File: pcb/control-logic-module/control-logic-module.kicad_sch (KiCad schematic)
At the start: 47 parts, among them U1 74HC04, U2 74AHC1G00, U3 74AHC1G00, U4 TLC556, U5 74LS145, Y1 8MHz

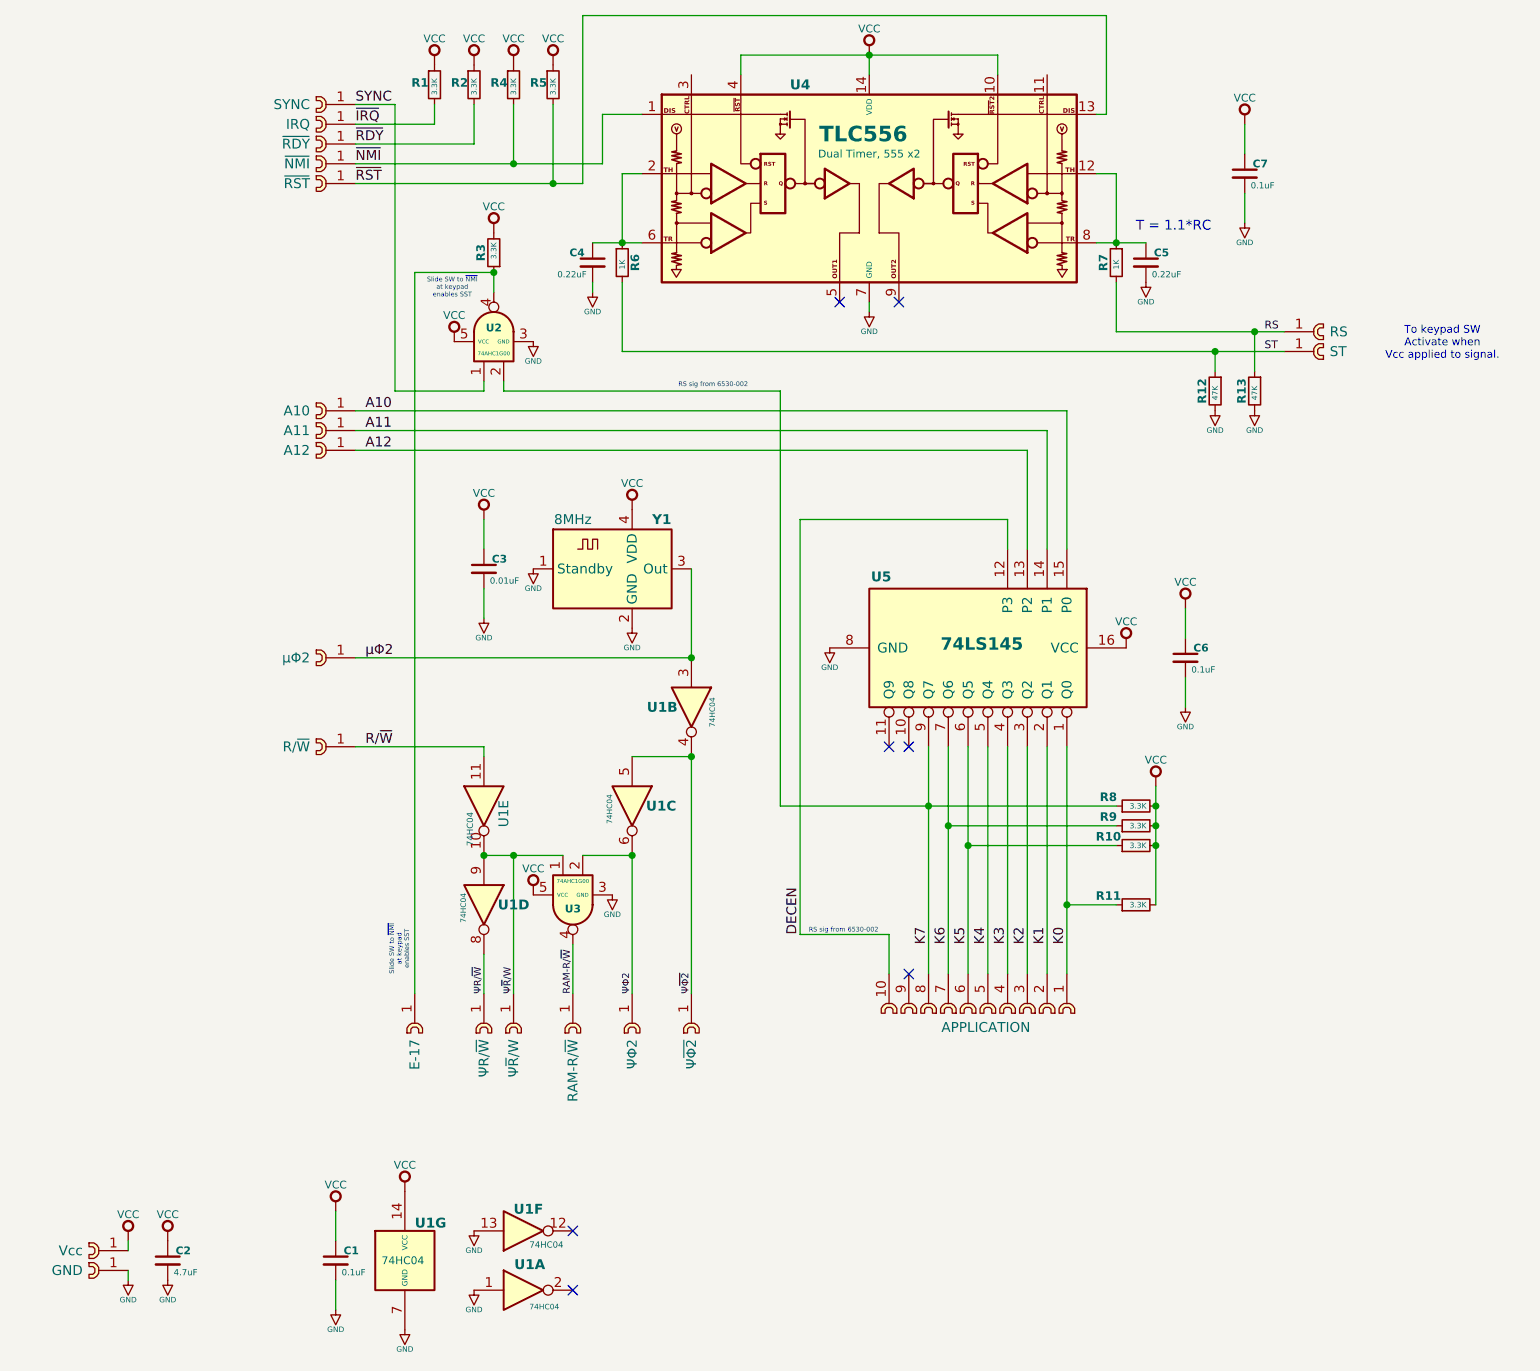
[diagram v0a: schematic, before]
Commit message: Fix ERC Errors
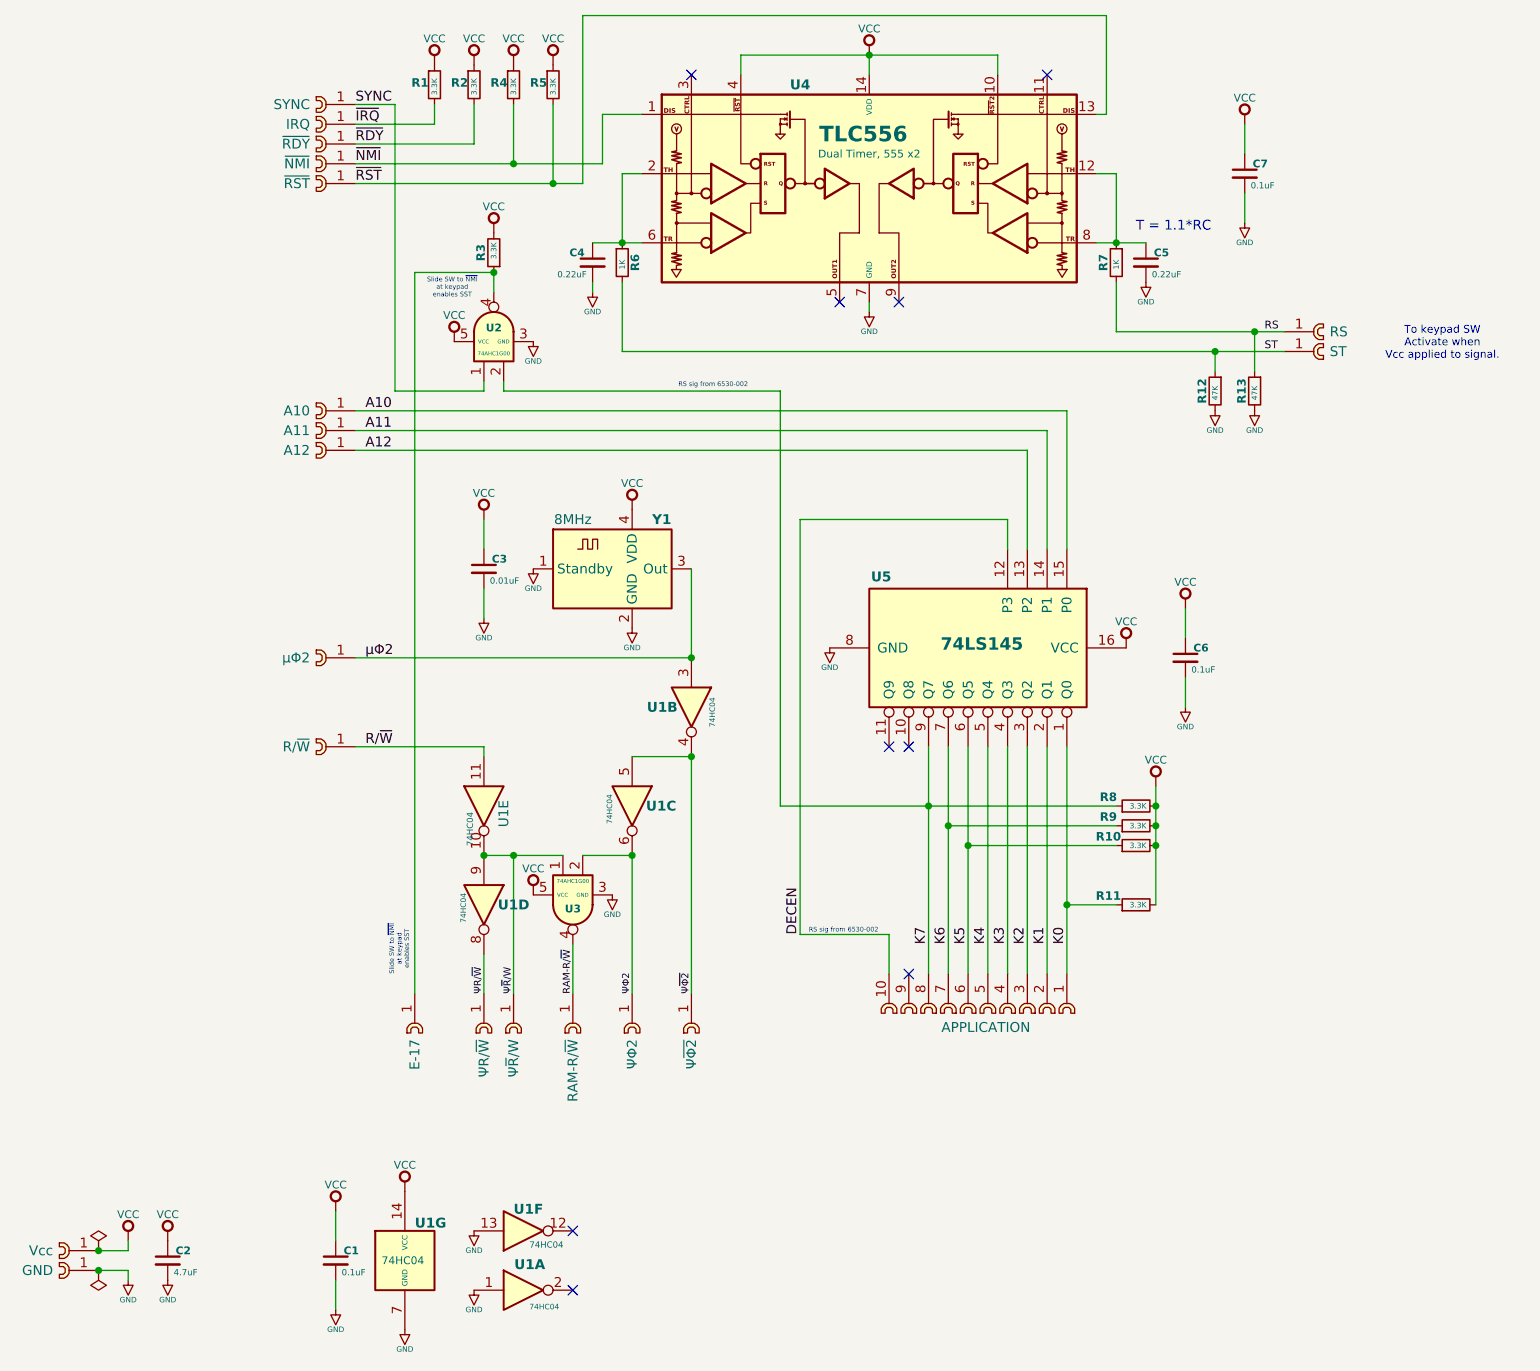
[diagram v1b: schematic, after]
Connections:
- no-connect marks 7 -> 9
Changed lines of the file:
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@@
 	)
 	(junction
+		(at 63.5 182.88)
+		(diameter 0)
+		(color 0 0 0 0)
+	)
+	(junction
 		(at 175.26 128.27)
 		(diameter 0)
@@
 	)
 	(junction
+		(at 63.5 180.34)
+		(diameter 0)
+		(color 0 0 0 0)
+	)
+	(junction
 		(at 113.03 129.54)
 		(diameter 0)
@@
 	)
 	(no_connect
+		(at 139.7 29.21)
+	)
+	(no_connect
 		(at 165.1 115.57)
 	)
@@
 	)
 	(no_connect
+		(at 185.42 29.21)
+	)
+	(no_connect
 		(at 124.46 177.8)
 	)
@@
 	(wire
 		(pts
-			(xy 67.31 184.15) (xy 67.31 182.88)
+			(xy 93.98 184.15) (xy 93.98 187.96)
 		)
 		(stroke
@@
 	(wire
 		(pts
-			(xy 93.98 184.15) (xy 93.98 187.96)
+			(xy 130.81 64.77) (xy 207.01 64.77)
 		)
 		(stroke
@@
 	(wire
 		(pts
-			(xy 130.81 64.77) (xy 207.01 64.77)
+			(xy 67.31 180.34) (xy 67.31 179.07)
 		)
 		(stroke
@@
 	(wire
 		(pts
+			(xy 67.31 182.88) (xy 67.31 184.15)
+		)
+		(stroke
+			(width 0)
+			(type default)
+		)
+	)
+	(wire
+		(pts
 			(xy 128.27 34.29) (xy 128.27 40.64)
 		)
@@
 	(wire
 		(pts
+			(xy 63.5 182.88) (xy 67.31 182.88)
+		)
+		(stroke
+			(width 0)
+			(type default)
+		)
+	)
+	(wire
+		(pts
 			(xy 182.88 77.47) (xy 182.88 90.17)
 		)
@@
 	(wire
 		(pts
+			(xy 63.5 180.34) (xy 67.31 180.34)
+		)
+		(stroke
+			(width 0)
+			(type default)
+		)
+	)
+	(wire
+		(pts
 			(xy 180.34 90.17) (xy 180.34 86.36)
 		)
@@
 	(wire
 		(pts
-			(xy 67.31 179.07) (xy 67.31 180.34)
-		)
-		(stroke
-			(width 0)
-			(type default)
-		)
-	)
-	(wire
-		(pts
 			(xy 106.68 33.02) (xy 106.68 35.56)
 		)
@@
 	)
 	(symbol
+		(lib_id "power:PWR_FLAG")
+		(at 63.5 180.34 0)
+		(unit 1)
+		(exclude_from_sim no)
+		(in_bom yes)
+		(on_board yes)
+		(dnp no)
+		(fields_autoplaced yes)
+		(property "Reference" "#FLG01"
+			(at 63.5 178.435 0)
+			(effects
+				(font
+					(size 1.27 1.27)
+				)
+				(hide yes)
+			)
+		)
+		(property "Value" "PWR_FLAG"
+			(at 63.5 175.26 0)
+			(effects
+				(font
+					(size 1.27 1.27)
+				)
+				(hide yes)
+			)
+		)
+		(property "Footprint" ""
+			(at 63.5 180.34 0)
+			(effects
+				(font
+					(size 1.27 1.27)
+				)
+				(hide yes)
+			)
+		)
+		(property "Datasheet" "~"
+			(at 63.5 180.34 0)
+			(effects
+				(font
+					(size 1.27 1.27)
+				)
+				(hide yes)
+			)
+		)
+		(property "Description" "Special symbol for telling ERC where power comes from"
+			(at 63.5 180.34 0)
+			(effects
+				(font
+					(size 1.27 1.27)
+				)
+				(hide yes)
+			)
+		)
+		(pin "1"
+		)
+		(instances
+			(project ""
+				(path "/4ebd6183-7c5f-46b0-b04d-0ff005f0292d"
+					(reference "#FLG01")
+					(unit 1)
+				)
+			)
+		)
+	)
+	(symbol
 		(lib_id "CM_power:VCC")
 		(at 114.3 49.53 0)
@@
 	(symbol
 		(lib_id "CM_Connector_Generic:cast-01")
-		(at 64.77 180.34 0)
+		(at 60.96 180.34 0)
 		(unit 1)
 		(exclude_from_sim no)
@@
 		(dnp no)
 		(property "Reference" "CST1"
-			(at 59.69 180.34 0)
+			(at 55.88 180.34 0)
 			(do_not_autoplace yes)
 			(effects
@@
 		)
 		(property "Value" "Vcc"
-			(at 61.468 180.34 0)
+			(at 57.658 180.34 0)
 			(effects
 				(font
@@
 		)
 		(property "Footprint" "CM_Connector_Castelated:cast-2.0-01P"
-			(at 57.15 180.34 0)
+			(at 53.34 180.34 0)
 			(do_not_autoplace yes)
 			(effects
@@
 		)
 		(property "Datasheet" ""
-			(at 64.77 180.34 0)
+			(at 60.96 180.34 0)
 			(effects
 				(font
@@
 		)
 		(property "Description" "Castelated PCB Edge - 2.0mm - 1P"
-			(at 57.15 179.07 0)
+			(at 53.34 179.07 0)
 			(do_not_autoplace yes)
 			(effects
@@
 	(symbol
 		(lib_id "CM_Connector_Generic:cast-01")
-		(at 64.77 182.88 0)
+		(at 60.96 182.88 0)
 		(unit 1)
 		(exclude_from_sim no)
@@
 		(dnp no)
 		(property "Reference" "CST2"
-			(at 59.69 182.88 0)
+			(at 55.88 182.88 0)
 			(do_not_autoplace yes)
 			(effects
@@
 		)
 		(property "Value" "GND"
-			(at 61.468 182.88 0)
+			(at 57.658 182.88 0)
 			(effects
 				(font
@@
 		)
 		(property "Footprint" "CM_Connector_Castelated:cast-2.0-01P"
-			(at 57.15 182.88 0)
+			(at 53.34 182.88 0)
 			(do_not_autoplace yes)
 			(effects
@@
 		)
 		(property "Datasheet" ""
-			(at 64.77 182.88 0)
+			(at 60.96 182.88 0)
 			(effects
 				(font
@@
 		)
 		(property "Description" "Castelated PCB Edge - 2.0mm - 1P"
-			(at 57.15 181.61 0)
+			(at 53.34 181.61 0)
 			(do_not_autoplace yes)
 			(effects
@@
 					(unit 1)
 				)
+			)
+		)
+	)
+	(symbol
+		(lib_id "power:PWR_FLAG")
+		(at 63.5 182.88 180)
+		(unit 1)
+		(exclude_from_sim no)
+		(in_bom yes)
+		(on_board yes)
+		(dnp no)
+		(fields_autoplaced yes)
+		(property "Reference" "#FLG02"
+			(at 63.5 184.785 0)
+			(effects
+				(font
+					(size 1.27 1.27)
+				)
+				(hide yes)
+			)
+		)
+		(property "Value" "PWR_FLAG"
+			(at 63.5 187.96 0)
+			(effects
+				(font
+					(size 1.27 1.27)
+				)
+				(hide yes)
+			)
+		)
+		(property "Footprint" ""
+			(at 63.5 182.88 0)
+			(effects
+				(font
+					(size 1.27 1.27)
+				)
+				(hide yes)
+			)
+		)
+		(property "Datasheet" "~"
+			(at 63.5 182.88 0)
+			(effects
+				(font
+					(size 1.27 1.27)
+				)
+				(hide yes)
+			)
+		)
+		(property "Description" "Special symbol for telling ERC where power comes from"
+			(at 63.5 182.88 0)
+			(effects
+				(font
+					(size 1.27 1.27)
+				)
+				(hide yes)
+			)
+		)
+		(pin "1"
+		)
+		(instances
+			(project "control-logic-module"
+				(path "/4ebd6183-7c5f-46b0-b04d-0ff005f0292d"
+					(reference "#FLG02")
+					(unit 1)
+				)

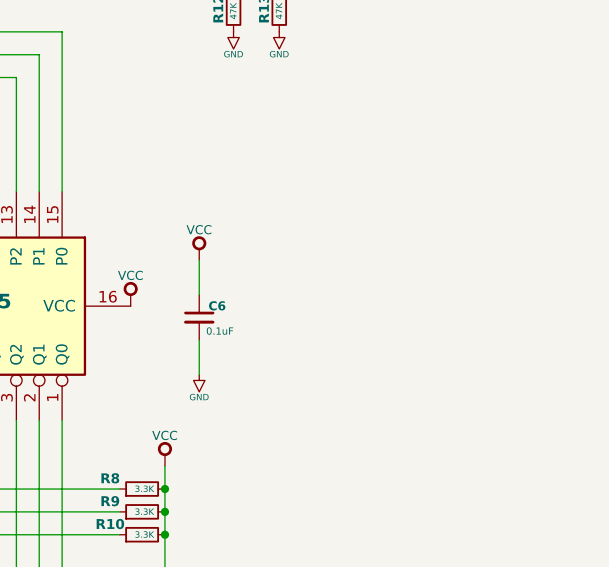
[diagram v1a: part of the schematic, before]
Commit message: Added assembly notes for future changes.
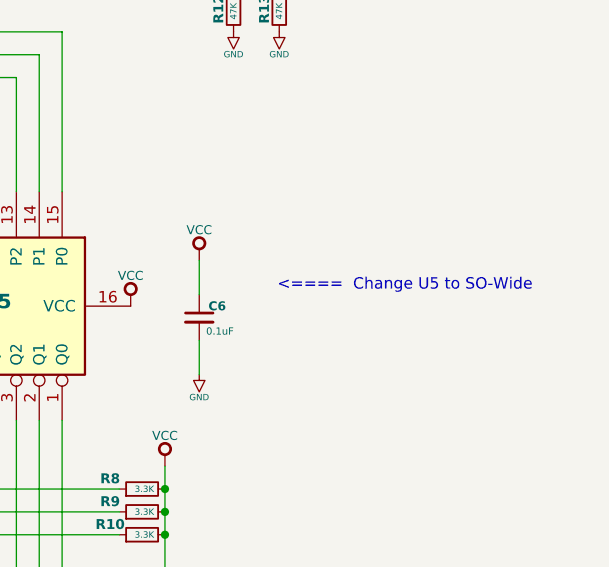
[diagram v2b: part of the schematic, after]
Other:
- note added: "<==== Change U5 to SO-Wide"
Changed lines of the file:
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@@
+		)
+	)
+	(text "<====  Change U5 to SO-Wide"
+		(exclude_from_sim no)
+		(at 226.06 100.584 0)
+		(effects
+			(font
+				(size 1.27 1.27)
+			)
 		)
 	)

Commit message: Make some corrections. Bump Rev to B.
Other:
- note added: "Open Standby pin for normal operation."
- company: (none) -> by Circuit Monkey
- title: (none) -> KIM-1000 Control Module
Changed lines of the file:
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@@
 	(generator_version "9.0")
 	(paper "A4")
+	(title_block
+		(title "KIM-1000 Control Module")
+		(date "2025-09-02")
+		(rev "B")
+		(company "by Circuit Monkey")
+	)
 	(text "RS sig from 6530-002"
 		(exclude_from_sim no)
@@
 		(effects
 			(font
+				(size 1.27 1.27)
+			)
+		)
+	)
+	(text "Open Standby pin for normal operation."
+		(exclude_from_sim no)
+		(at 127.762 81.026 0)
+		(effects
+			(font

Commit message: Update and finalize rev-b board.
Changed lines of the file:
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@@
 	(title_block
 		(title "KIM-1000 Control Module")
-		(date "2025-09-02")
+		(date "2025-09-21")
 		(rev "B")
 		(company "by Circuit Monkey")
@@
 		(dnp no)
 		(property "Reference" "U1"
-			(at 133.858 123.19 90)
+			(at 127.762 121.666 0)
 			(do_not_autoplace yes)
 			(effects
@@
 		(dnp no)
 		(property "Reference" "U1"
-			(at 114.808 135.89 90)
+			(at 108.966 134.366 0)
 			(do_not_autoplace yes)
 			(effects
@@
 		(dnp no)
 		(property "Reference" "U1"
-			(at 137.922 110.49 90)
+			(at 135.636 112.522 0)
 			(do_not_autoplace yes)
 			(effects
@@
 		)
 		(property "Value" "74HC04"
-			(at 141.986 109.22 0)
+			(at 136.652 108.458 0)
 			(effects
 				(font
@@
 		(dnp no)
 		(property "Reference" "U1"
-			(at 115.57 122.428 0)
+			(at 108.966 121.666 0)
 			(effects
 				(font
 					(size 1.27 1.27)
+					(thickness 0.254)
+					(bold yes)
 				)
 				(justify left)
@@
 		)
 		(property "Value" "74HC04"
-			(at 111.252 123.952 0)
+			(at 110.49 121.412 0)
 			(effects
 				(font

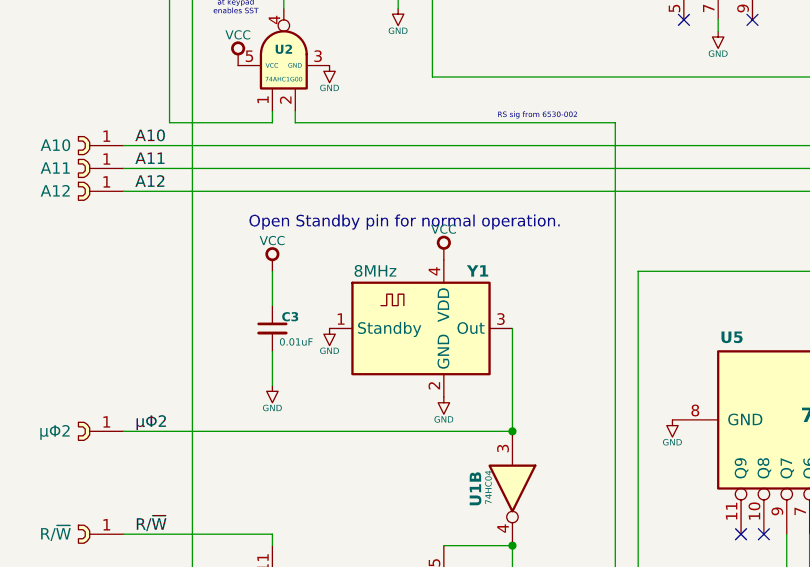
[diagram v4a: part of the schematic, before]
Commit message: Add changes for Rev.C.  Clock pin connection issue.
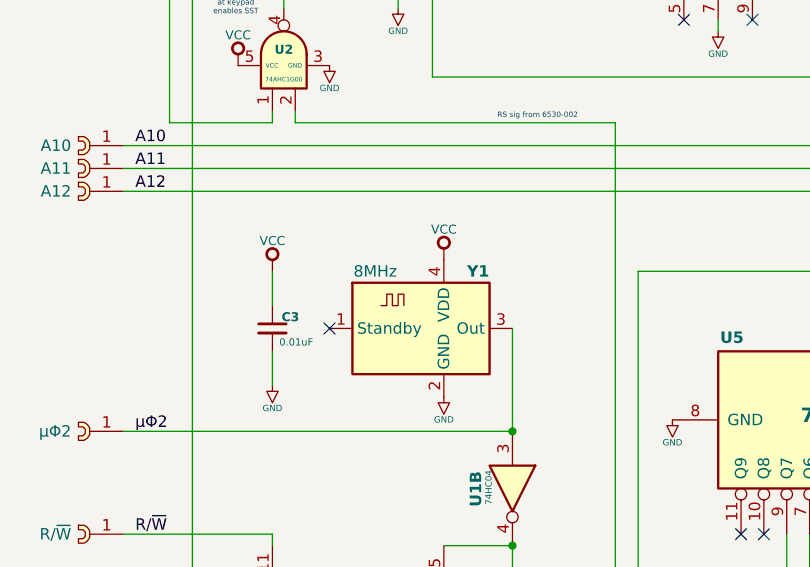
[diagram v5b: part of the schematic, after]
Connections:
- net GND: no longer Y1.1 (Standby)
- no-connect marks 9 -> 10
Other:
- note removed: "Open Standby pin for normal operation."
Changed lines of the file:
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@@
 		(title "KIM-1000 Control Module")
 		(date "2025-09-21")
-		(rev "B")
+		(rev "C")
 		(company "by Circuit Monkey")
 	)
@@
 		)
 	)
-	(text "Open Standby pin for normal operation."
-		(exclude_from_sim no)
-		(at 127.762 81.026 0)
-		(effects
-			(font
-				(size 1.27 1.27)
-			)
-		)
-	)
 	(text "Slide SW to ~{NMI} \nat keypad \nenables SST"
 		(exclude_from_sim no)
@@
 	)
 	(no_connect
+		(at 119.38 92.71)
+	)
+	(no_connect
 		(at 124.46 185.42)
 	)
@@
 					(unit 1)
 				)
-			)
-		)
-	)
-	(symbol
-		(lib_id "CM_power:GND")
-		(at 119.38 92.71 0)
-		(unit 1)
-		(exclude_from_sim no)
-		(in_bom yes)
-		(on_board yes)
-		(dnp no)
-		(fields_autoplaced yes)
-		(property "Reference" "#PWR019"
-			(at 119.38 99.06 0)
-			(effects
-				(font
-					(size 1.27 1.27)
-				)
-				(hide yes)
-			)
-		)
-		(property "Value" "GND"
-			(at 119.38 94.81 0)
-			(do_not_autoplace yes)
-			(effects
-				(font
-					(size 0.7 0.7)
-				)
-				(justify top)
-			)
-		)
-		(property "Footprint" ""
-			(at 119.38 92.71 0)
-			(effects
-				(font
-					(size 1.27 1.27)
-				)
-				(hide yes)
-			)
-		)
-		(property "Datasheet" ""
-			(at 119.38 92.71 0)
-			(effects
-				(font
-					(size 1.27 1.27)
-				)
-				(hide yes)
-			)
-		)
-		(property "Description" "Power symbol creates a global label with name \"GND\" , ground"
-			(at 119.38 92.71 0)
-			(effects
-				(font
-					(size 1.27 1.27)
-				)
-				(hide yes)
-			)
-		)
-		(pin "1"
-		)
-		(instances
-			(project "control-logic-module"
-				(path "/4ebd6183-7c5f-46b0-b04d-0ff005f0292d"
-					(reference "#PWR019")
-					(unit 1)
-				)
